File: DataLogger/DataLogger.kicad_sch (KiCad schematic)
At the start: 0 parts

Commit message: added components in schematic
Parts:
- added BT1: Battery, symbol Device:Battery
- added C1, C2, C3, C4: C, symbol Device:C
- added C5: C_Polarized, symbol Device:C_Polarized
- added D1, D2: LED, symbol Device:LED
- added H1, H2, H3, H4: MountingHole, symbol Mechanical:MountingHole
- added R1, R2, R3, R4, R5, R6, R7: R, symbol Device:R
- added U1, U2: 24LC1025, symbol Memory_EEPROM:24LC1025
- added Y1, Y2: Crystal, symbol Device:Crystal
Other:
- title: (none) -> MCU Datalogger

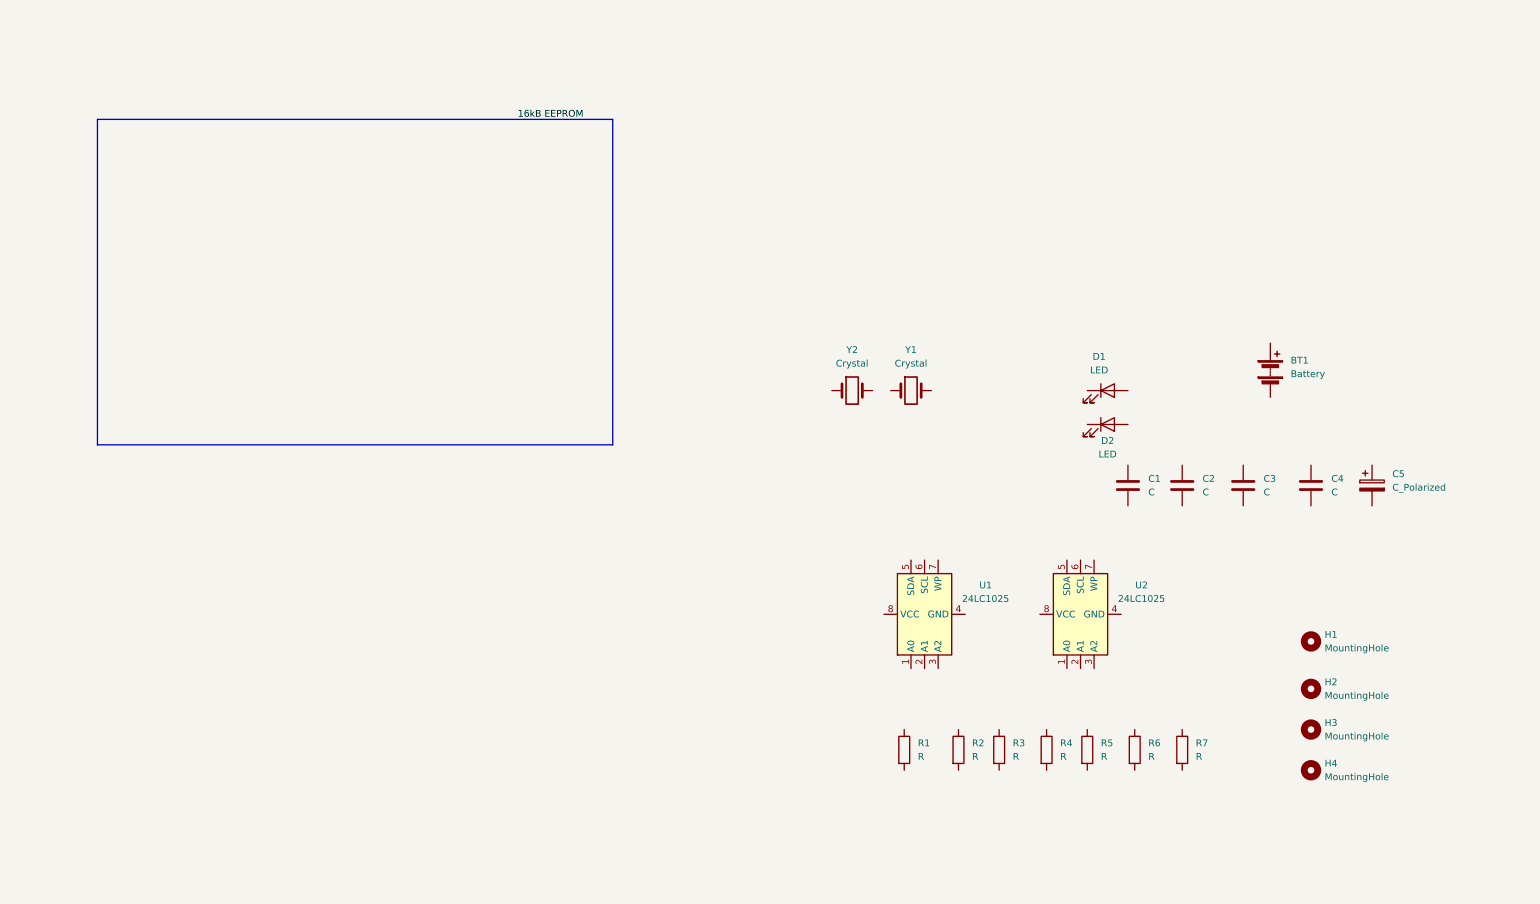
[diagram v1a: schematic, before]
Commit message: found footprints for atmega & ds1337s+
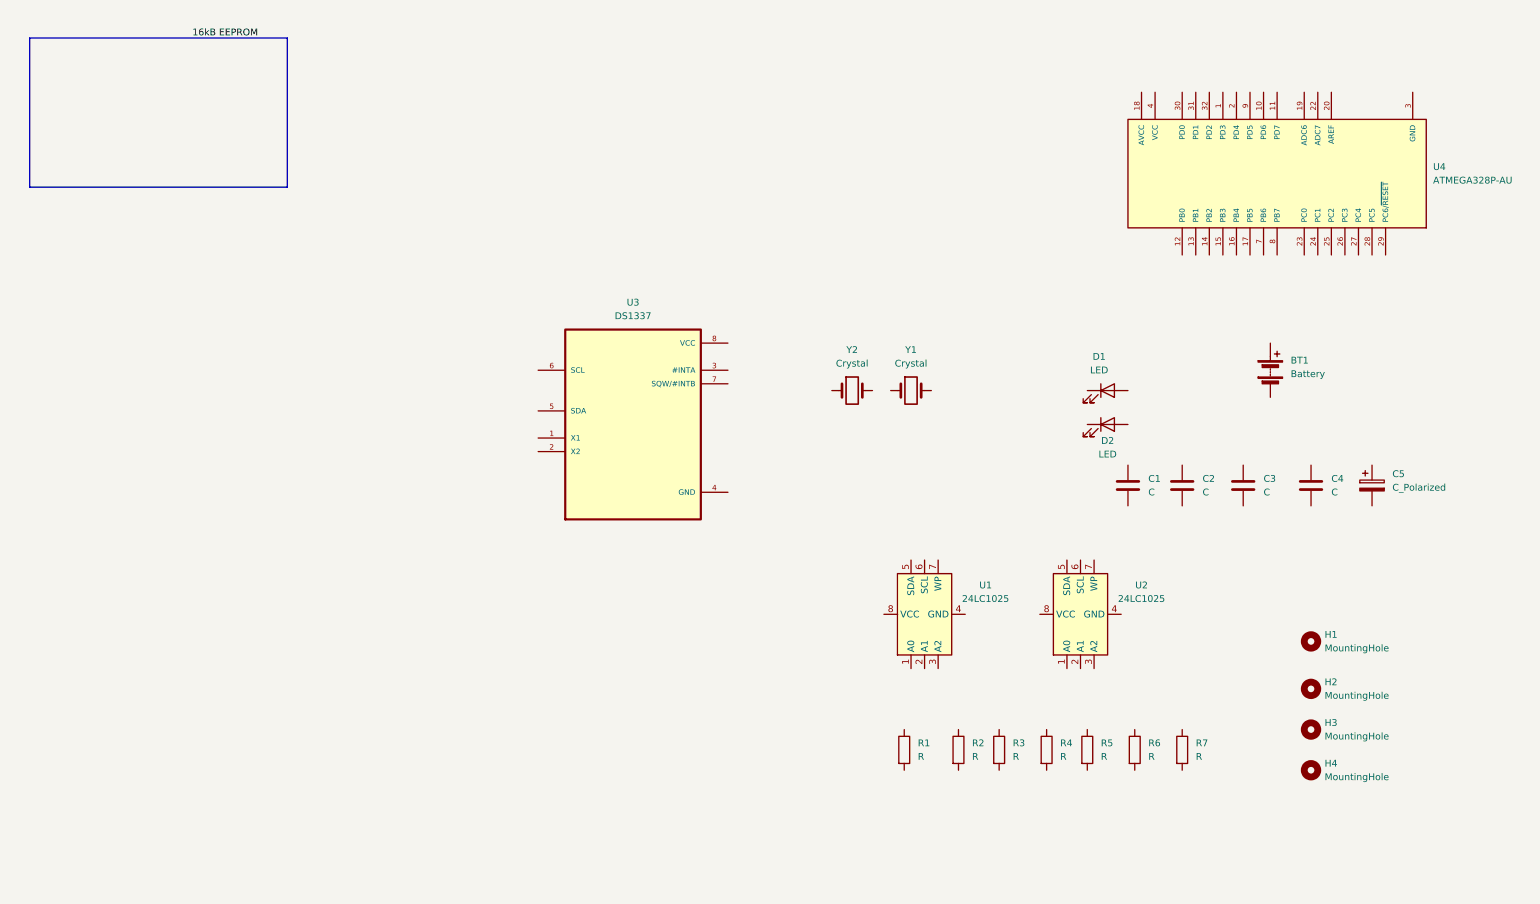
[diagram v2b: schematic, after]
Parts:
- added U3: DS1337, DS1337:DIP794W47P254L991H457Q8, symbol DS1337:DS1337
- added U4: ATMEGA328P-AU, ATMEGA328P-AU:QFP80P900X900X120-32N, symbol ATMEGA328P-AU:ATMEGA328P-AU
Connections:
- new net GND: U4.21 (GND), U4.3 (GND), U4.5 (GND)
- new net VCC: U4.4 (VCC), U4.6 (VCC)

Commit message: more
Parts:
- C1, C4: value C -> 0.1uF
- C2, C3: value C -> 22pF
- C5: value C_Polarized -> 100nF
- R1, R5, R6: value R -> 10k
- R2, R7: value R -> 330
- R3, R4: value R -> 4.7k
- Y1: value Crystal -> 32.768
- Y2: value Crystal -> 16MHz
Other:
- added sheet Conn (connectors.kicad_sch)
- moved on the sheet: BT1, C1, C2, C3, C4, C5, D1, D2, R1, R2, R3, R4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

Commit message: traces traced
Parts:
- BT1: footprint (none) -> Battery:BatteryHolder_Keystone_103_1x20mm
- C1: footprint (none) -> Capacitor_SMD:C_1210_3225Metric
- C2, C3, C4: footprint (none) -> Capacitor_SMD:C_0201_0603Metric
- C5: footprint (none) -> Capacitor_SMD:CP_Elec_4x3
- D1: footprint (none) -> LED_SMD:LED_0201_0603Metric
- D2: footprint (none) -> LED_SMD:LED_1210_3225Metric
- H1, H2, H3, H4: footprint (none) -> MountingHole:MountingHole_2.1mm
- R1, R2, R3, R4, R5, R6, R7: footprint (none) -> Resistor_SMD:R_0805_2012Metric
- U1, U2: footprint (none) -> Package_SO:SOIC-8_3.9x4.9mm_P1.27mm
- Y1: value 32.768 -> 32.768 KHz; footprint (none) -> Crystal:Crystal_SMD_5032-2Pin_5.0x3.2mm
- Y2: footprint (none) -> Crystal:Crystal_SMD_5032-2Pin_5.0x3.2mm
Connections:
- net GND: now also BT1.2 (-), C1.2, C2.1, C3.1, C4.2, C5.2, D2.1 (K), R2.1, U1.4 (GND), U1.7 (WP), U2.2 (A1), U2.4 (GND), U2.7 (WP), U3.4 (GND)
- net VCC: now also C1.1, R1.1, R3.1, R4.1, R5.1, R6.1, U1.1 (A0), U1.2 (A1), U1.3 (A2), U1.8 (VCC), U2.1 (A0), U2.3 (A2), U2.8 (VCC), U3.8 (VCC); no longer U4.4 (VCC), U4.6 (VCC)
- net at R1.2: now also U4.29 (PC6/~{RESET})
- net at Y1.1: now also U3.1 (X1)
- net at Y1.2: now also U3.2 (X2)
- net at U4.17 (PB5): now also R7.2
- net at U4.18 (AVCC): now also BT1.1 (+), C5.1, D1.2 (A), U4.4 (VCC)
- net at U4.20 (AREF): now also C4.1
- net at U4.7 (PB6): now also C3.2, Y2.2
- net at U4.8 (PB7): now also C2.2, Y2.1
- net at R5.2: now also U3.3 (#INTA)
- net at R6.2: now also U3.7 (SQW/#INTB)
- net at R7.1: now also D2.2 (A)
- net at D1.1 (K): now also R2.2
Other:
- moved on the sheet: BT1, C2, C3, C4, C5, D1, D2, R2, R7, U1, U2, Y1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
